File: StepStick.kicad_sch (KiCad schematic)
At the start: 6 parts, among them J701 Conn_02x03_Odd_Even, J702 Conn_01x08_Female, J703 Screw_Terminal_01x04, J705 Conn_01x08_Female

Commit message: Place motor drivers, start layout of Ethernet PHY
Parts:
- J1402: renamed from J703; footprint TerminalBlock_Phoenix:TerminalBlock_Phoenix_PT-1,5-4-5.0-H_1x04_P5.00mm_Horizontal -> TerminalBlock_Phoenix:TerminalBlock_Phoenix_MPT-0,5-4-2.54_1x04_P2.54mm_Horizontal
- renumbered C701 to C1401, J702 to J1401, J701 to J1403, J705 to J1404, R701 to R1401
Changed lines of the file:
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@@
-(kicad_sch (version 20200618) (host eeschema "5.99.0-unknown-77313e4~101~ubuntu20.04.1")
-  (page 7 14)
+(kicad_sch (version 20200618) (host eeschema "5.99.0-unknown-7340c97~102~ubuntu20.04.1")
+  (page 10 14)
   (paper "B")
   (title_block
@@
   (symbol (lib_id "power:+24V") (at 180.34 95.25 0)
     (in_bom yes) (on_board yes)
-    (property "Reference" "#PWR0701" (id 0) (at 180.34 99.06 0)
+    (property "Reference" "#PWR01401" (id 0) (at 180.34 99.06 0)
       (effects (font (size 1.27 1.27)) hide)
     )
@@
   (symbol (lib_id "power:+3V3") (at 182.88 80.01 0)
     (in_bom yes) (on_board yes)
-    (property "Reference" "#PWR0702" (id 0) (at 182.88 83.82 0)
+    (property "Reference" "#PWR01402" (id 0) (at 182.88 83.82 0)
       (effects (font (size 1.27 1.27)) hide)
     )
@@
   (symbol (lib_id "power:+3V3") (at 220.98 156.21 0)
     (in_bom yes) (on_board yes)
-    (property "Reference" "#PWR0704" (id 0) (at 220.98 160.02 0)
+    (property "Reference" "#PWR01405" (id 0) (at 220.98 160.02 0)
       (effects (font (size 1.27 1.27)) hide)
     )
@@
   (symbol (lib_id "power:+3V3") (at 238.76 86.36 0)
     (in_bom yes) (on_board yes)
-    (property "Reference" "#PWR0107" (id 0) (at 238.76 90.17 0)
+    (property "Reference" "#PWR01406" (id 0) (at 238.76 90.17 0)
       (effects (font (size 1.27 1.27)) hide)
     )
@@
   (symbol (lib_id "power:GNDD") (at 199.39 171.45 0)
     (in_bom yes) (on_board yes)
-    (property "Reference" "#PWR0703" (id 0) (at 199.39 177.8 0)
+    (property "Reference" "#PWR01404" (id 0) (at 199.39 177.8 0)
       (effects (font (size 1.27 1.27)) hide)
     )
@@
   (symbol (lib_id "power:GND") (at 189.23 106.68 0)
     (in_bom yes) (on_board yes)
-    (property "Reference" "#PWR0106" (id 0) (at 189.23 113.03 0)
+    (property "Reference" "#PWR01403" (id 0) (at 189.23 113.03 0)
       (effects (font (size 1.27 1.27)) hide)
     )
@@
   (symbol (lib_id "Device:R_Small_US") (at 238.76 91.44 0)
     (in_bom yes) (on_board yes)
-    (property "Reference" "R701" (id 0) (at 240.4111 90.2906 0)
+    (property "Reference" "R1401" (id 0) (at 240.4111 90.2906 0)
       (effects (font (size 1.27 1.27)) (justify left))
     )
@@
   (symbol (lib_id "Device:CP1") (at 189.23 101.6 0)
     (in_bom yes) (on_board yes)
-    (property "Reference" "C701" (id 0) (at 192.1511 100.4506 0)
+    (property "Reference" "C1401" (id 0) (at 192.1511 100.4506 0)
       (effects (font (size 1.27 1.27)) (justify left))
     )
@@
   (symbol (lib_id "Connector:Screw_Terminal_01x04") (at 207.01 204.47 0)
     (in_bom yes) (on_board yes)
-    (property "Reference" "J703" (id 0) (at 209.0421 204.6414 0)
+    (property "Reference" "J1402" (id 0) (at 209.0421 204.6414 0)
       (effects (font (size 1.27 1.27)) (justify left))
     )
@@
       (effects (font (size 1.27 1.27)) (justify left))
     )
-    (property "Footprint" "TerminalBlock_Phoenix:TerminalBlock_Phoenix_PT-1,5-4-5.0-H_1x04_P5.00mm_Horizontal" (id 2) (at 207.01 204.47 0)
+    (property "Footprint" "TerminalBlock_Phoenix:TerminalBlock_Phoenix_MPT-0,5-4-2.54_1x04_P2.54mm_Horizontal" (id 2) (at 207.01 204.47 0)
       (effects (font (size 1.27 1.27)) hide)
     )
@@
   (symbol (lib_id "Connector_Generic:Conn_02x03_Odd_Even") (at 210.82 162.56 0)
     (in_bom yes) (on_board yes)
-    (property "Reference" "J701" (id 0) (at 212.09 154.5398 0))
+    (property "Reference" "J1403" (id 0) (at 212.09 154.5398 0))
     (property "Value" "Conn_02x03_Odd_Even" (id 1) (at 212.09 170.18 0))
     (property "Footprint" "Connector_PinHeader_2.54mm:PinHeader_2x03_P2.54mm_Vertical" (id 2) (at 210.82 162.56 0)
@@
   (symbol (lib_id "Connector:Conn_01x08_Female") (at 199.39 86.36 0)
     (in_bom yes) (on_board yes)
-    (property "Reference" "J702" (id 0) (at 195.58 72.39 0)
+    (property "Reference" "J1401" (id 0) (at 195.58 72.39 0)
       (effects (font (size 1.27 1.27)) (justify left))
     )
@@
   (symbol (lib_id "Connector:Conn_01x08_Female") (at 217.17 86.36 0) (mirror y)
     (in_bom yes) (on_board yes)
-    (property "Reference" "J705" (id 0) (at 219.8624 72.8026 0))
+    (property "Reference" "J1404" (id 0) (at 219.8624 72.8026 0))
     (property "Value" "Conn_01x08_Female" (id 1) (at 219.8624 75.1013 0))
     (property "Footprint" "Connector_PinSocket_2.54mm:PinSocket_1x08_P2.54mm_Vertical" (id 2) (at 217.17 86.36 0)

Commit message: Add FTDI chip
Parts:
- renumbered C1401 to C1501, J1401 to J1501, J1402 to J1502, J1403 to J1503, J1404 to J1504, R1401 to R1501
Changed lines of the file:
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@@
-(kicad_sch (version 20200618) (host eeschema "5.99.0-unknown-7340c97~102~ubuntu20.04.1")
-  (page 10 14)
+(kicad_sch (version 20200618) (host eeschema "5.99.0-unknown-e9da02e~102~ubuntu20.04.1")
+  (page 15 15)
   (paper "B")
   (title_block
@@
   (symbol (lib_id "power:+24V") (at 180.34 95.25 0)
     (in_bom yes) (on_board yes)
-    (property "Reference" "#PWR01401" (id 0) (at 180.34 99.06 0)
+    (property "Reference" "#PWR01501" (id 0) (at 180.34 99.06 0)
       (effects (font (size 1.27 1.27)) hide)
     )
@@
   (symbol (lib_id "power:+3V3") (at 182.88 80.01 0)
     (in_bom yes) (on_board yes)
-    (property "Reference" "#PWR01402" (id 0) (at 182.88 83.82 0)
+    (property "Reference" "#PWR01502" (id 0) (at 182.88 83.82 0)
       (effects (font (size 1.27 1.27)) hide)
     )
@@
   (symbol (lib_id "power:+3V3") (at 220.98 156.21 0)
     (in_bom yes) (on_board yes)
-    (property "Reference" "#PWR01405" (id 0) (at 220.98 160.02 0)
+    (property "Reference" "#PWR01505" (id 0) (at 220.98 160.02 0)
       (effects (font (size 1.27 1.27)) hide)
     )
@@
   (symbol (lib_id "power:+3V3") (at 238.76 86.36 0)
     (in_bom yes) (on_board yes)
-    (property "Reference" "#PWR01406" (id 0) (at 238.76 90.17 0)
+    (property "Reference" "#PWR01506" (id 0) (at 238.76 90.17 0)
       (effects (font (size 1.27 1.27)) hide)
     )
@@
   (symbol (lib_id "power:GNDD") (at 199.39 171.45 0)
     (in_bom yes) (on_board yes)
-    (property "Reference" "#PWR01404" (id 0) (at 199.39 177.8 0)
+    (property "Reference" "#PWR01504" (id 0) (at 199.39 177.8 0)
       (effects (font (size 1.27 1.27)) hide)
     )
@@
   (symbol (lib_id "power:GND") (at 189.23 106.68 0)
     (in_bom yes) (on_board yes)
-    (property "Reference" "#PWR01403" (id 0) (at 189.23 113.03 0)
+    (property "Reference" "#PWR01503" (id 0) (at 189.23 113.03 0)
       (effects (font (size 1.27 1.27)) hide)
     )
@@
   (symbol (lib_id "Device:R_Small_US") (at 238.76 91.44 0)
     (in_bom yes) (on_board yes)
-    (property "Reference" "R1401" (id 0) (at 240.4111 90.2906 0)
+    (property "Reference" "R1501" (id 0) (at 240.4111 90.2906 0)
       (effects (font (size 1.27 1.27)) (justify left))
     )
@@
   (symbol (lib_id "Device:CP1") (at 189.23 101.6 0)
     (in_bom yes) (on_board yes)
-    (property "Reference" "C1401" (id 0) (at 192.1511 100.4506 0)
+    (property "Reference" "C1501" (id 0) (at 192.1511 100.4506 0)
       (effects (font (size 1.27 1.27)) (justify left))
     )
@@
   (symbol (lib_id "Connector:Screw_Terminal_01x04") (at 207.01 204.47 0)
     (in_bom yes) (on_board yes)
-    (property "Reference" "J1402" (id 0) (at 209.0421 204.6414 0)
+    (property "Reference" "J1502" (id 0) (at 209.0421 204.6414 0)
       (effects (font (size 1.27 1.27)) (justify left))
     )
@@
   (symbol (lib_id "Connector_Generic:Conn_02x03_Odd_Even") (at 210.82 162.56 0)
     (in_bom yes) (on_board yes)
-    (property "Reference" "J1403" (id 0) (at 212.09 154.5398 0))
+    (property "Reference" "J1503" (id 0) (at 212.09 154.5398 0))
     (property "Value" "Conn_02x03_Odd_Even" (id 1) (at 212.09 170.18 0))
     (property "Footprint" "Connector_PinHeader_2.54mm:PinHeader_2x03_P2.54mm_Vertical" (id 2) (at 210.82 162.56 0)
@@
   (symbol (lib_id "Connector:Conn_01x08_Female") (at 199.39 86.36 0)
     (in_bom yes) (on_board yes)
-    (property "Reference" "J1401" (id 0) (at 195.58 72.39 0)
+    (property "Reference" "J1501" (id 0) (at 195.58 72.39 0)
       (effects (font (size 1.27 1.27)) (justify left))
     )
@@
   (symbol (lib_id "Connector:Conn_01x08_Female") (at 217.17 86.36 0) (mirror y)
     (in_bom yes) (on_board yes)
-    (property "Reference" "J1404" (id 0) (at 219.8624 72.8026 0))
+    (property "Reference" "J1504" (id 0) (at 219.8624 72.8026 0))
     (property "Value" "Conn_01x08_Female" (id 1) (at 219.8624 75.1013 0))
     (property "Footprint" "Connector_PinSocket_2.54mm:PinSocket_1x08_P2.54mm_Vertical" (id 2) (at 217.17 86.36 0)

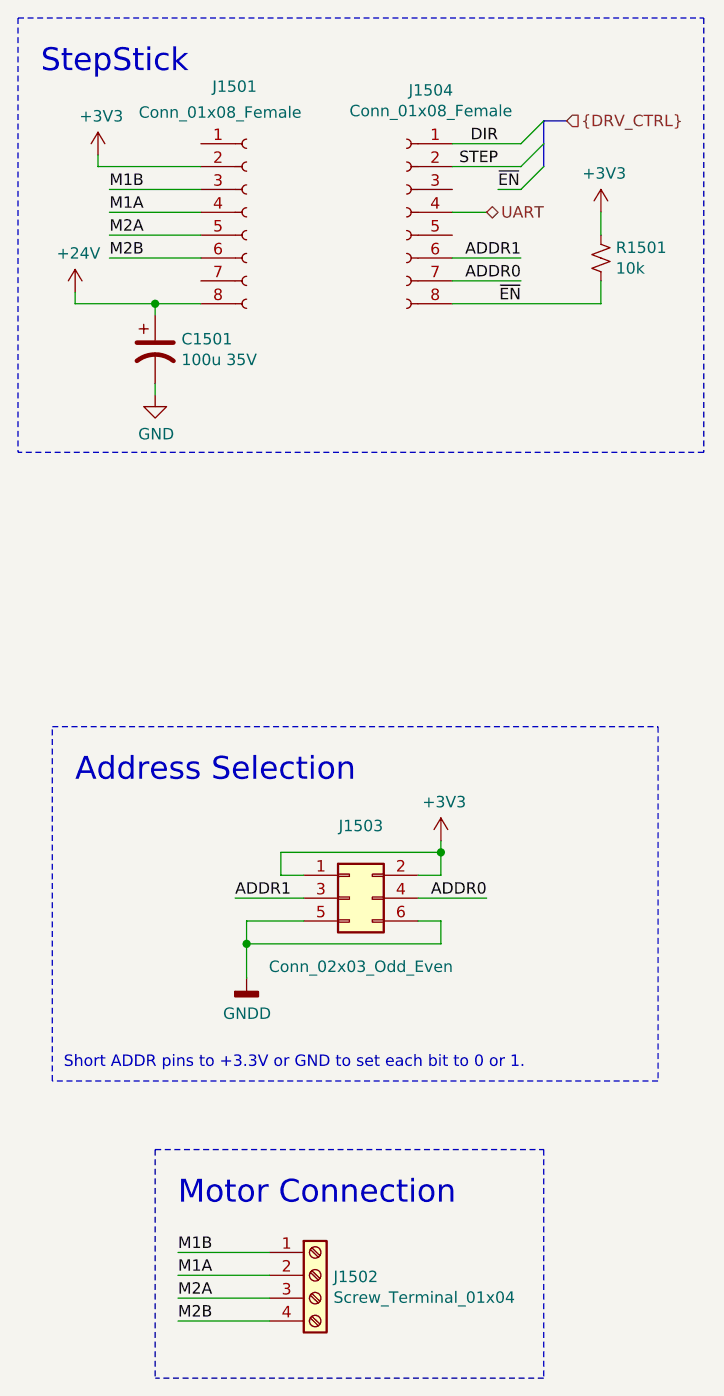
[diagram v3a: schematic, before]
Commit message: Attach ethernet to PL, layout and route
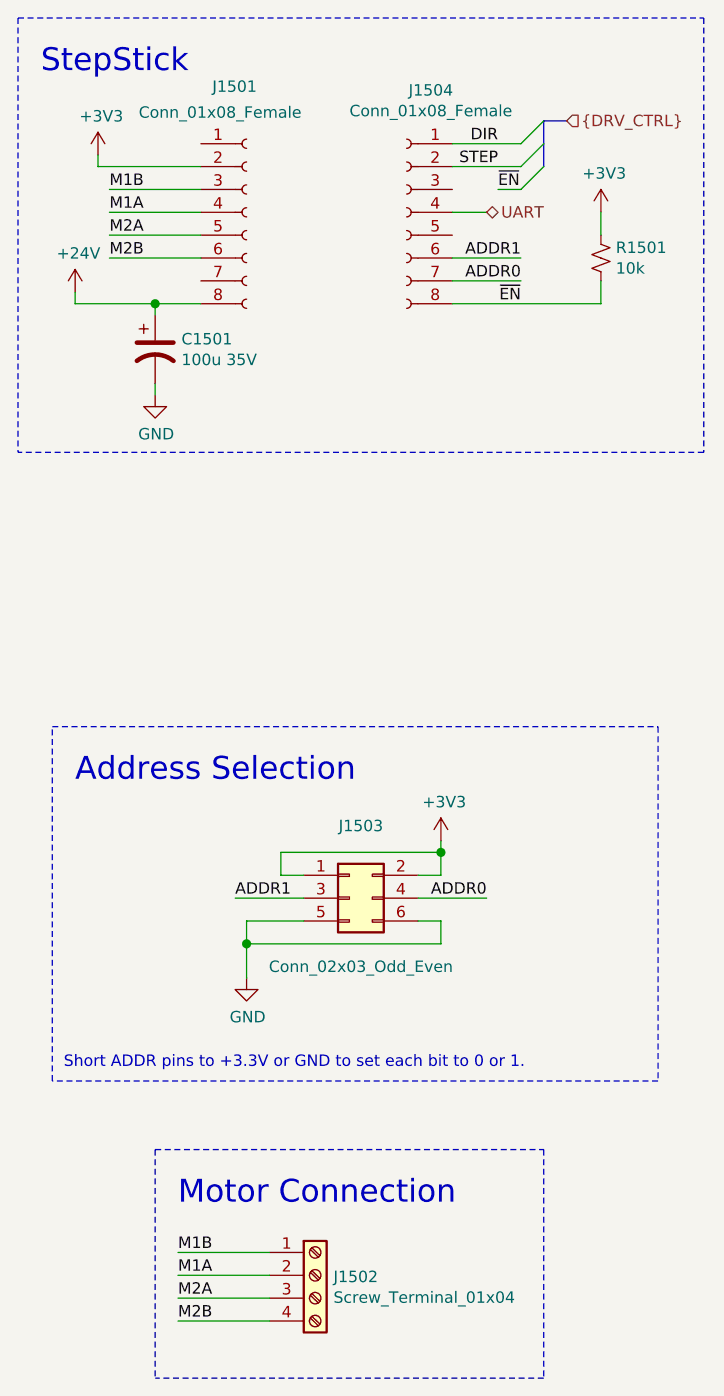
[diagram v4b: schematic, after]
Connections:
- net GNDD is gone; now on net GND: J1503.5 (Pin_5), J1503.6 (Pin_6)
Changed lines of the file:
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@@
-(kicad_sch (version 20200714) (host eeschema "5.99.0-unknown-bf445c1~102~ubuntu20.04.1")
-  (page 1 15)
+(kicad_sch (version 20200714) (host eeschema "5.99.0-unknown-a146cd9~102~ubuntu20.04.1")
+  (page 0 15)
   (paper "B")
   (title_block
@@
   )
   (bus_alias "DRV_CTRL" (members "STEP" "DIR" "~EN"))
-  (junction (at 189.23 96.52) (diameter 0) (color 0 0 0 0))
-  (junction (at 199.39 167.64) (diameter 0) (color 0 0 0 0))
-  (junction (at 220.98 157.48) (diameter 0) (color 0 0 0 0))
+  (junction (at 189.23 96.52) (diameter 1.016) (color 0 0 0 0))
+  (junction (at 199.39 167.64) (diameter 1.016) (color 0 0 0 0))
+  (junction (at 220.98 157.48) (diameter 1.016) (color 0 0 0 0))
   (bus_entry (at 229.87 78.74) (size 2.54 -2.54)
     (stroke (width 0.1524) (type solid) (color 0 0 0 0))
@@
     )
   )
-  (symbol (lib_id "power:GNDD") (at 199.39 171.45 0)
-    (in_bom yes) (on_board yes)
-    (property "Reference" "#PWR01504" (id 0) (at 199.39 177.8 0)
-      (effects (font (size 1.27 1.27)) hide)
-    )
-    (property "Value" "GNDD" (id 1) (at 199.4408 175.3934 0))
-    (property "Footprint" "" (id 2) (at 199.39 171.45 0)
-      (effects (font (size 1.27 1.27)) hide)
-    )
-    (property "Datasheet" "" (id 3) (at 199.39 171.45 0)
-      (effects (font (size 1.27 1.27)) hide)
-    )
-  )
   (symbol (lib_id "power:GND") (at 189.23 106.68 0)
     (in_bom yes) (on_board yes)
@@
       (effects (font (size 1.27 1.27)) hide)
     )
+  )
+  (symbol (lib_id "power:GND") (at 199.39 171.45 0)
+    (in_bom yes) (on_board yes)
+    (property "Reference" "#PWR0129" (id 0) (at 199.39 177.8 0)
+      (effects (font (size 1.27 1.27)) hide)
+    )
+    (property "Value" "GND" (id 1) (at 199.5043 175.7744 0))
+    (property "Footprint" "" (id 2) (at 199.39 171.45 0)
+      (effects (font (size 1.27 1.27)) hide)
+    )
+    (property "Datasheet" "" (id 3) (at 199.39 171.45 0)
+      (effects (font (size 1.27 1.27)) hide)
+    )

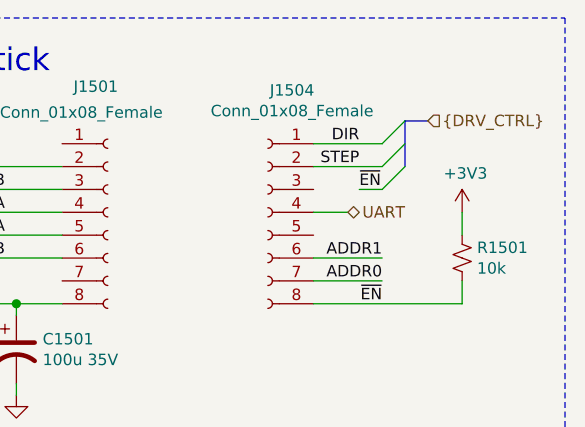
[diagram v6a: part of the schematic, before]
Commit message: Move Ethernet PHY to left side of board
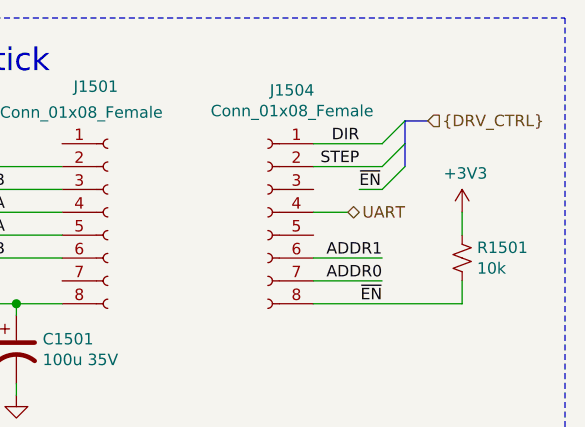
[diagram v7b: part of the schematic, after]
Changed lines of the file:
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@@
-(kicad_sch (version 20200714) (host eeschema "5.99.0-unknown-829316fad~102~ubuntu20.04.1")
+(kicad_sch (version 20200828) (generator eeschema)
   (page 0 15)
   (paper "B")
@@
     (stroke (width 0) (type solid) (color 0 0 0 0))
   )
-  (bus (pts (xy 232.41 76.2) (xy 232.41 81.28))
+  (bus (pts (xy 232.41 76.2) (xy 232.41 78.74))
     (stroke (width 0) (type solid) (color 0 0 0 0))
   )
@@
     (stroke (width 0) (type solid) (color 0 0 0 0))
   )
+  (bus (pts (xy 232.41 78.74) (xy 232.41 81.28))
+    (stroke (width 0) (type solid) (color 0 0 0 0))
+  )
